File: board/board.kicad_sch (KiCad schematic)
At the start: 8 parts, among them J1 023_LED, J2 023_LED

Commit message: Add footrpint, symbol and 3d model
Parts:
- D1: footprint LED_GW_J9LHS1.4M-C1C7-2+58+MQ+30A-1-100-R33 -> GW_J9LHS1:LED_GW_J9LHS1.4M-C1C7-2+58+MQ+30A-1-100-R33
- J1, J2: value 023_LED -> osf.011
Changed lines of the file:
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@@
     (in_bom yes) (on_board yes) (fields_autoplaced)
     (property "Reference" "J1" (id 0) (at 85.725 80.01 0))
-    (property "Value" "023_LED" (id 1) (at 85.725 82.55 0))
+    (property "Value" "osf.011" (id 1) (at 85.725 82.55 0))
     (property "Footprint" "on_edge:on_edge_2x05_device" (id 2) (at 77.47 81.28 0)
       (effects (font (size 1.27 1.27)) hide)
@@
       (effects (font (size 1.27 1.27)) (justify left))
     )
-    (property "Value" "023_LED" (id 1) (at 200.66 103.5049 0)
+    (property "Value" "osf.011" (id 1) (at 200.66 103.5049 0)
       (effects (font (size 1.27 1.27)) (justify left))
     )
@@
     (property "Reference" "D1" (id 0) (at 143.51 68.58 0))
     (property "Value" "GW_J9LHS1.4M-C1C7-2+58+MQ+30A-1-100-R33" (id 1) (at 142.24 71.12 0))
-    (property "Footprint" "LED_GW_J9LHS1.4M-C1C7-2+58+MQ+30A-1-100-R33" (id 2) (at 138.43 100.33 0)
+    (property "Footprint" "GW_J9LHS1:LED_GW_J9LHS1.4M-C1C7-2+58+MQ+30A-1-100-R33" (id 2) (at 138.43 100.33 0)
       (effects (font (size 1.27 1.27)) (justify bottom) hide)
     )
@@
   (symbol_instances
     (path "/a9ef1f92-a45b-4310-a6e9-4059abd051da"
-      (reference "D1") (unit 1) (value "GW_J9LHS1.4M-C1C7-2+58+MQ+30A-1-100-R33") (footprint "LED_GW_J9LHS1.4M-C1C7-2+58+MQ+30A-1-100-R33")
+      (reference "D1") (unit 1) (value "GW_J9LHS1.4M-C1C7-2+58+MQ+30A-1-100-R33") (footprint "GW_J9LHS1:LED_GW_J9LHS1.4M-C1C7-2+58+MQ+30A-1-100-R33")
     )
     (path "/02ab4736-fba1-4e6c-abef-aa7c088d94a7"
-      (reference "J1") (unit 1) (value "023_LED") (footprint "on_edge:on_edge_2x05_device")
+      (reference "J1") (unit 1) (value "osf.011") (footprint "on_edge:on_edge_2x05_device")
     )
     (path "/6169c5fa-dc29-45cd-8d2f-b575e54f7735"
-      (reference "J2") (unit 1) (value "023_LED") (footprint "on_edge:on_edge_2x05_host")
+      (reference "J2") (unit 1) (value "osf.011") (footprint "on_edge:on_edge_2x05_host")
     )
     (path "/b72b6f4a-7489-40f2-bb90-d75ae01aa368"

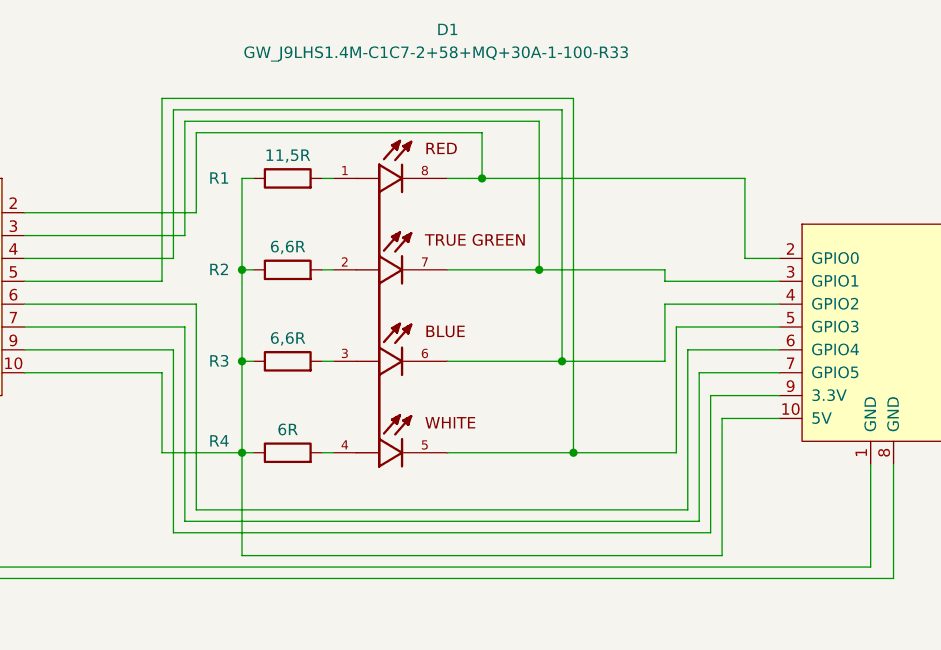
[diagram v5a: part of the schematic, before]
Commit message: Update Schmetaic Design for better heat management
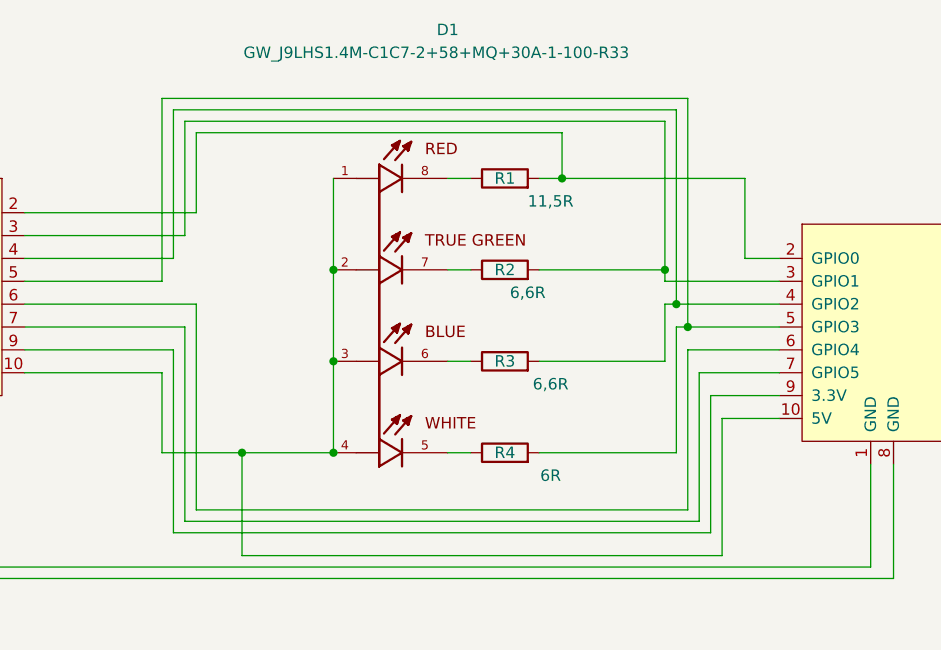
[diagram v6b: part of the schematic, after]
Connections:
- net at J1.2 (GPIO0), J2.2 (GPIO0): now also R1.2; no longer D1.8
- net at J1.3 (GPIO1), J2.3 (GPIO1): now also R2.2; no longer D1.7
- net at J1.4 (GPIO2), J2.4 (GPIO2): now also R3.2; no longer D1.6
- net at J1.5 (GPIO3), J2.5 (GPIO3): now also R4.2; no longer D1.5
- net at D1.3: now also D1.1, D1.2, D1.4, J1.10 (5V), J2.10 (5V); no longer R3.2
- new net: D1.6, R3.1
- new net: D1.8, R1.1
- new net: D1.7, R2.1
- new net: D1.5, R4.1
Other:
- moved on the sheet: R1, R2, R3, R4
